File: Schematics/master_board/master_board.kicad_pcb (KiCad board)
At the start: 2 copper layers, 156 x 156 mm, 74 parts, among them J1 2x5x1.27mm, J2 USB_C_Receptacle_USB2.0, J3 Conn_01x01_Female, J4 Conn_01x01_Female, J5 Conn_01x01_Female, J6 Conn_01x01_Female, M0 Conn_01x06_Male, M1 Conn_01x06_Male, M10 Conn_01x06_Male, M11 Conn_01x06_Male, M12 Conn_01x06_Male, M13 Conn_01x06_Male, M14 Conn_01x06_Male, M15 Conn_01x06_Male, M16 Conn_01x06_Male, M17 Conn_01x06_Male, M18 Conn_01x06_Male, M19 Conn_01x06_Male, M2 Conn_01x06_Male, M3 Conn_01x06_Male, M4 Conn_01x06_Male, M5 Conn_01x06_Male, M6 Conn_01x06_Male, M7 Conn_01x06_Male, M8 Conn_01x06_Male, M9 Conn_01x06_Male, SW1 SW_Push, SW2 SW_Push, SW3 SW_Push, U1 NCP1117-3.3_SOT223, U2 RP2040, U3 W25Q16JVSSIQ, U4 74HCT154PW,118, U5 74HCT154PW,118, Y1 ABLS-12.000MHZ-B4-T

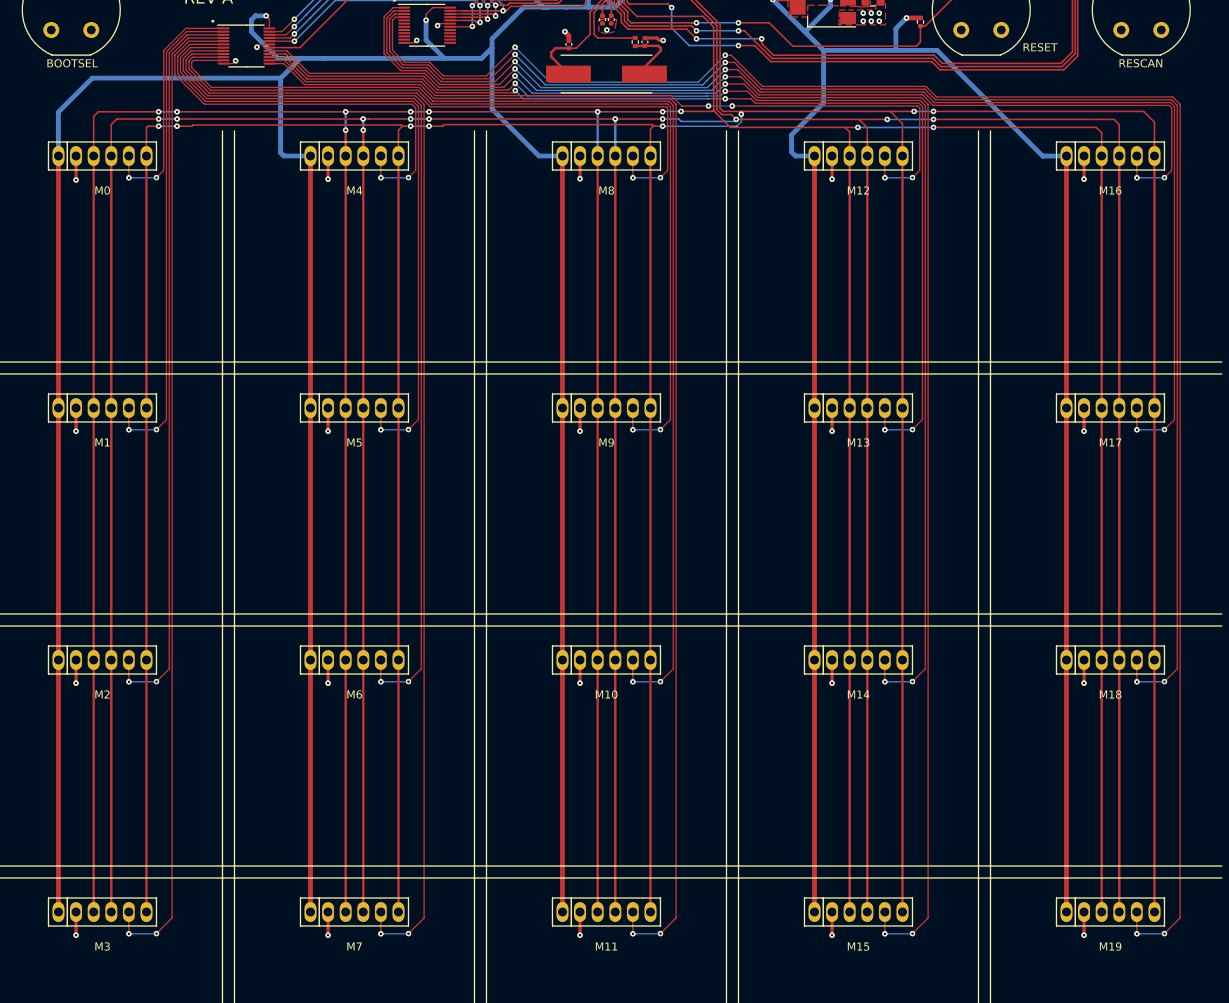
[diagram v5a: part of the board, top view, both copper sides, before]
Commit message: Shifted pogo-pins up by 0.25mm
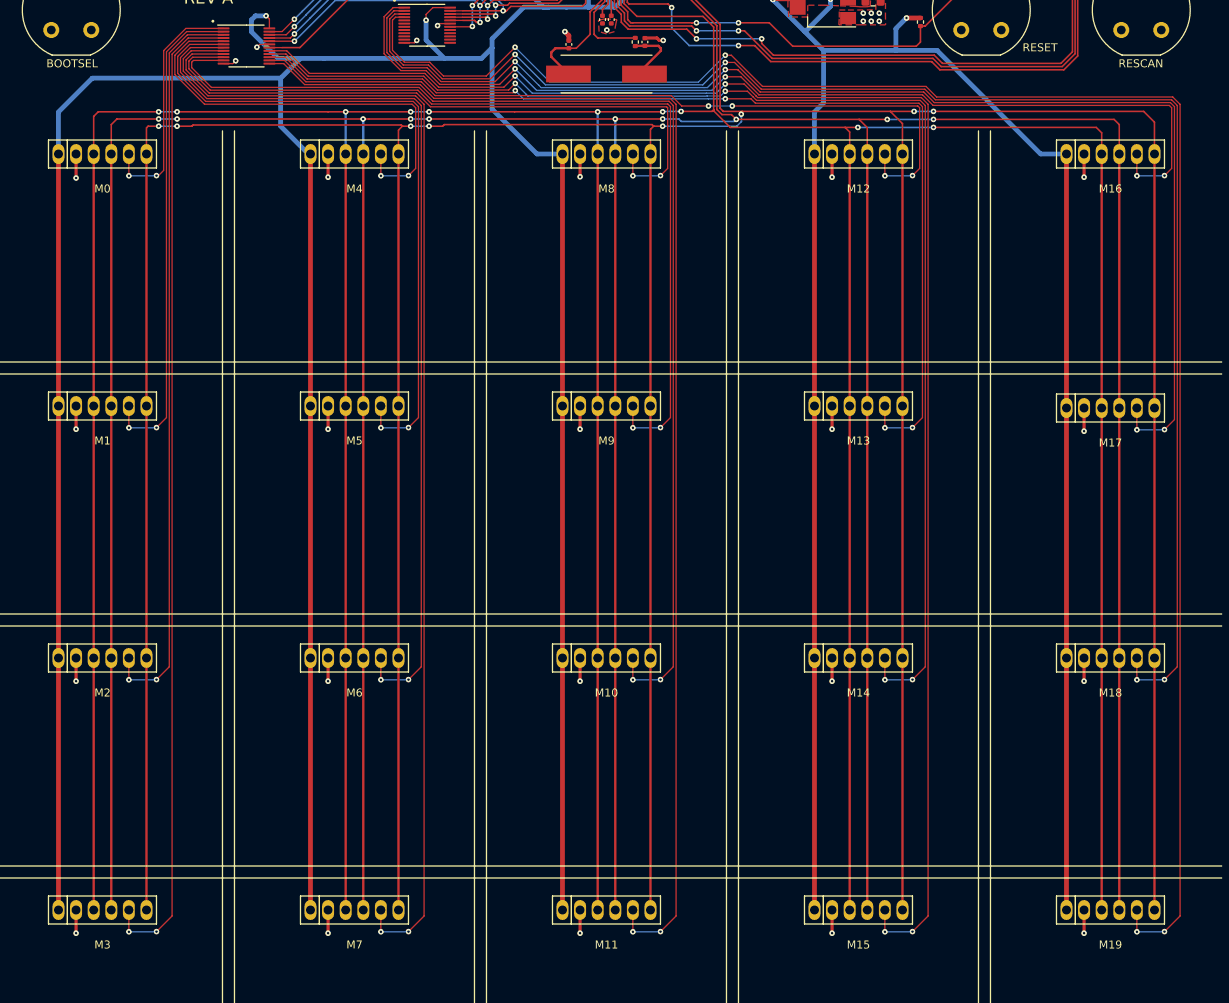
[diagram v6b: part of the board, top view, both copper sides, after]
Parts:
- moved M0 0.25 mm to (32.0, 53.5)
- moved M1 0.25 mm to (32.0, 85.0)
- moved M10 0.25 mm to (95.0, 116.5)
- moved M11 0.25 mm to (95.0, 148.0)
- moved M12 0.25 mm to (126.5, 53.5)
- moved M13 0.25 mm to (126.5, 85.0)
- moved M14 0.25 mm to (126.5, 116.5)
- moved M15 0.25 mm to (126.5, 148.0)
- moved M16 0.25 mm to (158.0, 53.5)
- moved M18 0.25 mm to (158.0, 116.5)
- moved M19 0.25 mm to (158.0, 148.0)
- moved M2 0.25 mm to (32.0, 116.5)
- moved M3 0.25 mm to (32.0, 148.0)
- moved M4 0.25 mm to (63.5, 53.5)
- moved M5 0.25 mm to (63.5, 85.0)
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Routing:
- net +3V3: track 883.8 -> 877.0 mm
- net SPI0_TX: track 648.9 -> 647.6 mm
- net SPI0_RX: track 646.5 -> 645.8 mm, vias 11 -> 10
- net SPI0_SCLK: track 647.1 -> 646.3 mm, vias 11 -> 10
